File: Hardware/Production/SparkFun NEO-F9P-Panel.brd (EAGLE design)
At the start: 160.8 x 107.4 mm, 768 parts, among them J1 ANTENNA-SMA-GROUNDEDEDGE_SMA, J11 ANTENNA-SMA-GROUNDEDEDGE_SMA, J15 Qwiic Right Angle, J16 Qwiic Right Angle, J18 ANTENNA-SMA-GROUNDEDEDGE_SMA, J2 Qwiic Right Angle, J22 Qwiic Right Angle, J23 Qwiic Right Angle, J25 ANTENNA-SMA-GROUNDEDEDGE_SMA, J29 Qwiic Right Angle, J30 Qwiic Right Angle, J32 ANTENNA-SMA-GROUNDEDEDGE_SMA, J36 Qwiic Right Angle, J37 Qwiic Right Angle, J39 ANTENNA-SMA-GROUNDEDEDGE_SMA, J4 Qwiic Right Angle, J6 Qwiic Right Angle, J9 Qwiic Right Angle, U1 U-BLOX_NEO-F9P-15B, U10 U-BLOX_NEO-F9P-15B, U11 3.3V, U12 U-BLOX_NEO-F9P-15B, U2 3.3V, U3 3.3V, U4 U-BLOX_NEO-F9P-15B, U5 3.3V, U6 U-BLOX_NEO-F9P-15B, U7 3.3V, U8 U-BLOX_NEO-F9P-15B, U9 3.3V

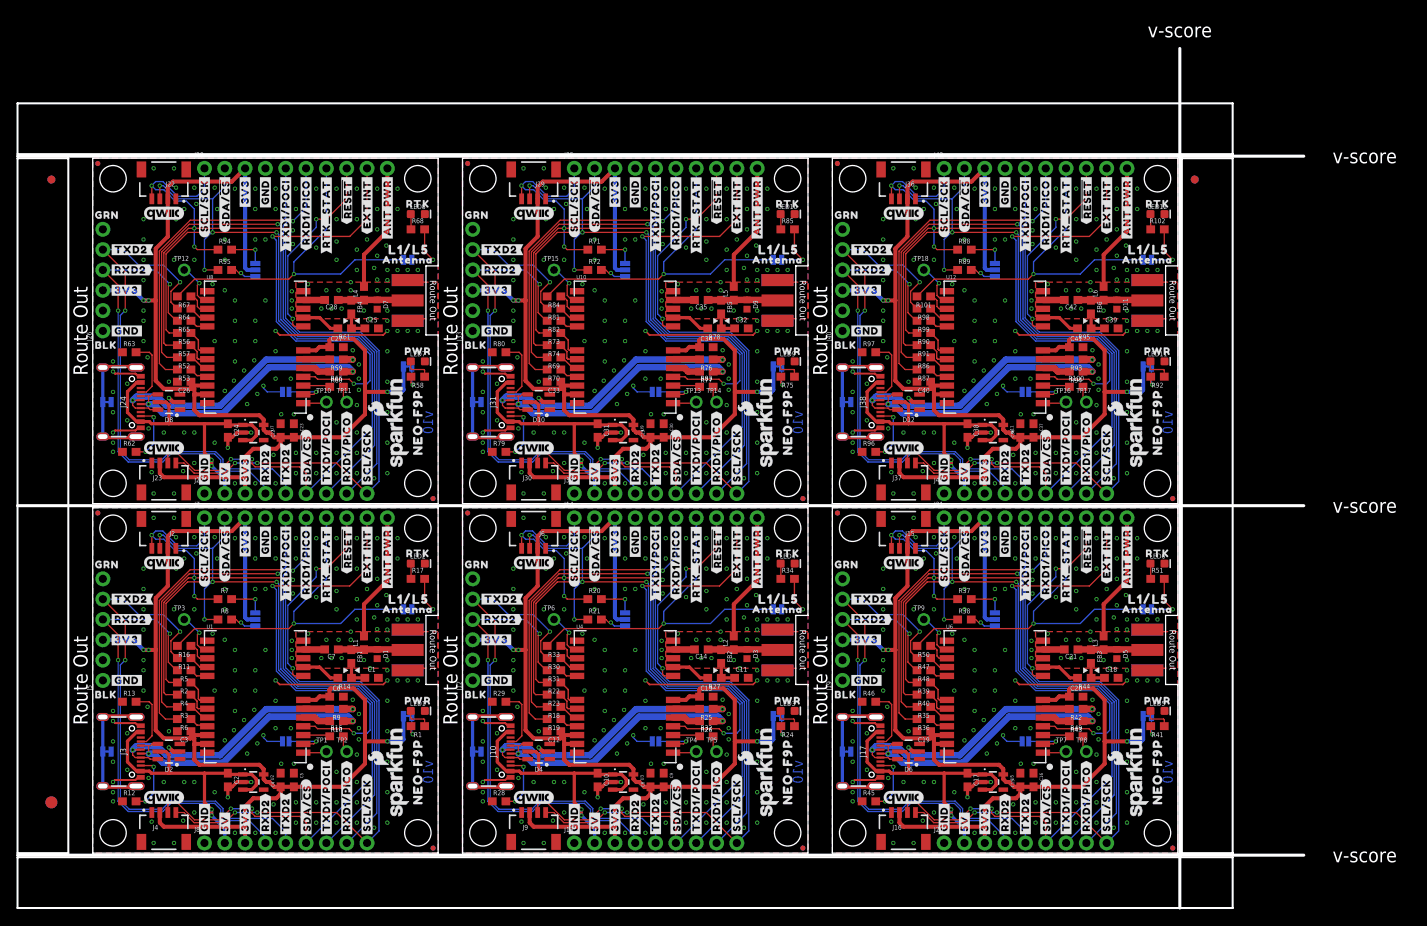
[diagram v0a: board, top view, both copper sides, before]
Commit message: Add backup batt. Add PPS LED and PTH. Change silk. Fix RTK LED.
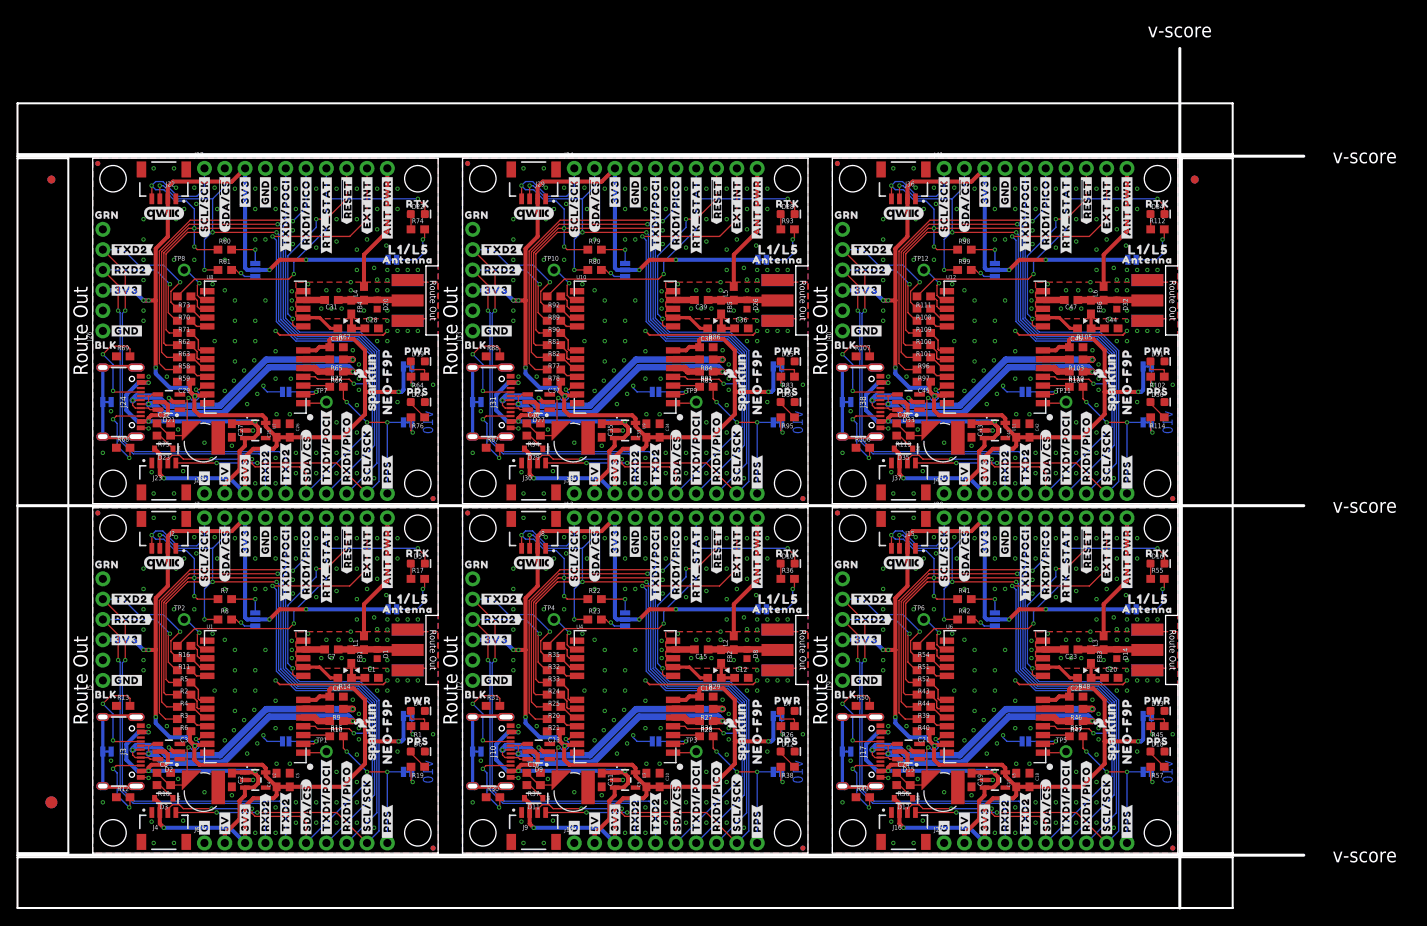
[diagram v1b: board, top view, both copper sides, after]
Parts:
- removed LED1, LED2, LED3, LED4: RED, SparkFun-LED:LED-0603
- removed LOGO25, LOGO29, LOGO30: QWIIC_LOGO_5MM, SparkFun-Aesthetics:QWIIC_5MM
- removed LOGO26, LOGO27: SFE_LOGO_NAME_FLAME.1_INCH, SparkFun-Aesthetics:SFE_LOGO_NAME_FLAME_.1
- removed LOGO28: OSHW-LOGOS, SparkFun-Aesthetics:OSHW-LOGO-S
- removed PWR\10, PWR\11, PWR\6, PWR\7, PWR\8, PWR\9: JUMPER-SMT_2_NC_TRACE_SILK, SparkFun-Jumpers:SMT-JUMPER_2_NC_TRACE_SILK
- removed TP13, TP14, TP15, TP16, TP17, TP18: TEST-POINTPOGO_PTH, SparkFun-Connectors:1X01_NO_SILK
- added B1, B2, B3, B4, B5, B6: 6.8MM_COIN_CELL, SparkFun-Batteries:ML414H_IV01E
- added C43, C45, C46, C48: 1.0uF, SparkFun-Capacitors:0603
- added C44, C47: 47pF, SparkFun-Capacitors:0603@1
- added D14, D20, D26, D32: PESD0402-0402, SparkFun-DiscreteSemi:0402
- added D15, D21, D27, D33: ESD Diode, SparkFun-DiscreteSemi:SOT-23-6
- added D17, D23, D29, D35: 0.5A/40V/420mV, SparkFun-DiscreteSemi:SOD-323
- added D18, D24, D30, D36: Yellow, SparkFun-LED:LED-0603
- added PULSE, PULSE1, PULSE2, PULSE3, PULSE4, PULSE5, RTK, RTK1, RTK2, RTK3, RTK4, RTK5: JUMPER-SMT_2_NC_TRACE_SILK, SparkFun-Jumpers:SMT-JUMPER_2_NC_TRACE_SILK
- added R103, R104: 27, SparkFun-Resistors:0603@1
- added R105: 10, SparkFun-Resistors:0603@1
- added R106, R107: 5.1k, SparkFun-Resistors:0603@1
- added R108, R109, R110, R111: 33, SparkFun-Resistors:0603@1
- added R112, R114: 2.2k, SparkFun-Resistors:0603@1
- added R113: 1k, SparkFun-Resistors:0603
- added U$397, U$398: (no value), output:#RXD1#PICO#2
- added U$399, U$400: (no value), output:#3V3#0
- added U$401: (no value), output:#ANT_PWR#0
- added U$402: (no value), output:#ANT_PWR#1
- added U$403, U$404: (no value), output:NEO#F9P0
- added U$405: (no value), output:#RTK_STAT#0
- added U$406: (no value), output:#_RTK_STAT#0
- added U$407: (no value), output:RTK0
- added U$408: (no value), output:#RTK#0
- added U$409, U$411: (no value), output:L1#L50
- added U$410: (no value), output:ANTENNA0
- added U$412: (no value), output:GNSS_RTK0
- added U$413: (no value), output:RECEIVER0
- added U$414: (no value), output:#LNA_EN#0
- added U$415: (no value), output:PPS0
- added U$416: (no value), output:#PPS#0
- added U$417: (no value), output:#_PPS#0
- added U$418: (no value), output:#PPS_#0
- added U$419: (no value), output:##SAFE##0
- added U$420: (no value), output:#G#0
- C1, C28, C39, C5, C7: device SparkFun-Capacitors:0603 -> SparkFun-Capacitors:0603@1
- C10, C26, C34: value 1.0uF -> 0.1uF; device SparkFun-Capacitors:0603 -> SparkFun-Capacitors:0603@1
- C11, C14, C21, C25, C32, C35: value 47pF -> 1.0uF
- C12, C15, C20, C31, C36: value 1.0uF -> 47pF; device SparkFun-Capacitors:0603 -> SparkFun-Capacitors:0603@1
- C16, C30, C37, C9: value 0.1uF -> 1.0uF
- C18, C42: value 47pF -> 0.1uF; device SparkFun-Capacitors:0603 -> SparkFun-Capacitors:0603@1
- C23: value 0.1uF -> 47pF; device SparkFun-Capacitors:0603 -> SparkFun-Capacitors:0603@1
- D10: value ESD Diode -> Blue; device SparkFun-DiscreteSemi:SOT-23-6 -> SparkFun-LED:LED-0603
- D11, D3: value PESD0402-0402 -> 0.5A/40V/420mV; device SparkFun-DiscreteSemi:0402 -> SparkFun-DiscreteSemi:SOD-323
- D12, D6: value ESD Diode -> Yellow; device SparkFun-DiscreteSemi:SOT-23-6 -> SparkFun-LED:LED-0603
- D13, D19, D25, D31: value RED -> Red
- D16, D22, D28, D34: value RED -> Blue
- D4: value ESD Diode -> Red; device SparkFun-DiscreteSemi:SOT-23-6 -> SparkFun-LED:LED-0603
- D5: value PESD0402-0402 -> Blue; device SparkFun-DiscreteSemi:0402 -> SparkFun-LED:LED-0603
- D7: value PESD0402-0402 -> Red; device SparkFun-DiscreteSemi:0402 -> SparkFun-LED:LED-0603
- D8: value ESD Diode -> PESD0402-0402; device SparkFun-DiscreteSemi:SOT-23-6 -> SparkFun-DiscreteSemi:0402
- D9: value PESD0402-0402 -> ESD Diode; device SparkFun-DiscreteSemi:0402 -> SparkFun-DiscreteSemi:SOT-23-6
- J13, J20, J27, J34, J41: device SparkFun-Connectors:1X09_NO_SILK -> SparkFun-Connectors:1X10_NO_SILK
- J6: value Qwiic Right Angle -> (none); device SparkFun-Connectors:JST04_1MM_RA -> SparkFun-Connectors:1X10_NO_SILK
- J8: value (none) -> Qwiic Right Angle; device SparkFun-Connectors:1X09_NO_SILK -> SparkFun-Connectors:JST04_1MM_RA
- LOGO1, LOGO17, LOGO21, LOGO3: value SFE_LOGO_NAME_FLAME.1_INCH -> SFE_LOGO_NAME_FLAME7_MM; device SparkFun-Aesthetics:SFE_LOGO_NAME_FLAME_.1 -> SparkFun-Aesthetics:SFE_LOGO_NAME_FLAME_7MM
- LOGO10, LOGO14, LOGO6: value QWIIC_LOGO_5MM -> SFE_LOGO_NAME_FLAME.1_INCH; device SparkFun-Aesthetics:QWIIC_5MM -> SparkFun-Aesthetics:SFE_LOGO_NAME_FLAME_.1
- LOGO11, LOGO7: value SFE_LOGO_NAME_FLAME.1_INCH -> OSHW-LOGOS; device SparkFun-Aesthetics:SFE_LOGO_NAME_FLAME_.1 -> SparkFun-Aesthetics:OSHW-LOGO-S
- LOGO12, LOGO16: value SFE_LOGO_NAME_FLAME.1_INCH -> QWIIC_LOGO_5MM; device SparkFun-Aesthetics:SFE_LOGO_NAME_FLAME_.1 -> SparkFun-Aesthetics:QWIIC_5MM
- LOGO13: value OSHW-LOGOS -> SFE_LOGO_NAME_FLAME7_MM; device SparkFun-Aesthetics:OSHW-LOGO-S -> SparkFun-Aesthetics:SFE_LOGO_NAME_FLAME_7MM
- LOGO15, LOGO19: value QWIIC_LOGO_5MM -> OSHW-LOGOS; device SparkFun-Aesthetics:QWIIC_5MM -> SparkFun-Aesthetics:OSHW-LOGO-S
- LOGO18: value OSHW-LOGOS -> SFE_LOGO_NAME_FLAME.1_INCH; device SparkFun-Aesthetics:OSHW-LOGO-S -> SparkFun-Aesthetics:SFE_LOGO_NAME_FLAME_.1
- LOGO8: value OSHW-LOGOS -> QWIIC_LOGO_5MM; device SparkFun-Aesthetics:OSHW-LOGO-S -> SparkFun-Aesthetics:QWIIC_5MM
- LOGO9: value QWIIC_LOGO_5MM -> SFE_LOGO_NAME_FLAME7_MM; device SparkFun-Aesthetics:QWIIC_5MM -> SparkFun-Aesthetics:SFE_LOGO_NAME_FLAME_7MM
- R10, R100, R101, R11, R12, R13, R14, R15, R16, R2, R3, R32, R33, R35, R38, R39, R4, R40, R5, R52, R53, R55, R6, R7, R70, R73, R8, R81, R82, R9, R90, R91: device SparkFun-Resistors:0603 -> SparkFun-Resistors:0603@1
- R17, R41: value 1k -> 2.2k; device SparkFun-Resistors:0603 -> SparkFun-Resistors:0603@1
- R18, R56, R64, R83: value 33 -> 1k
- R19, R22, R23, R36, R57, R74, R98, R99: value 33 -> 2.2k; device SparkFun-Resistors:0603 -> SparkFun-Resistors:0603@1
- R20, R21, R54, R71, R72, R89: value 2.2k -> 33; device SparkFun-Resistors:0603 -> SparkFun-Resistors:0603@1
- R24, R34, R51, R58, R92: value 1k -> 33; device SparkFun-Resistors:0603 -> SparkFun-Resistors:0603@1
- R25, R43, R59, R77: value 27 -> 33; device SparkFun-Resistors:0603 -> SparkFun-Resistors:0603@1
- R26, R94: value 27 -> 1k
- R27: value 10 -> 27; device SparkFun-Resistors:0603 -> SparkFun-Resistors:0603@1
- R28, R46: value 5.1k -> 27; device SparkFun-Resistors:0603 -> SparkFun-Resistors:0603@1
- R29: value 5.1k -> 10; device SparkFun-Resistors:0603 -> SparkFun-Resistors:0603@1
- R30, R31, R49, R50, R69, R87: value 33 -> 5.1k; device SparkFun-Resistors:0603 -> SparkFun-Resistors:0603@1
- R37: value 2.2k -> 1k
- R42, R60, R76, R93: value 27 -> 2.2k; device SparkFun-Resistors:0603 -> SparkFun-Resistors:0603@1
- R44, R78: value 10 -> 33; device SparkFun-Resistors:0603 -> SparkFun-Resistors:0603@1
- R45: value 5.1k -> 1k
- R47, R65, R66, R84: value 33 -> 27; device SparkFun-Resistors:0603 -> SparkFun-Resistors:0603@1
- R48, R67, R86: value 33 -> 10; device SparkFun-Resistors:0603 -> SparkFun-Resistors:0603@1
- R61, R95: value 10 -> 2.2k; device SparkFun-Resistors:0603 -> SparkFun-Resistors:0603@1
- R62, R63, R96, R97: value 5.1k -> 33; device SparkFun-Resistors:0603 -> SparkFun-Resistors:0603@1
- R68: value 1k -> 5.1k; device SparkFun-Resistors:0603 -> SparkFun-Resistors:0603@1
- R79, R80: value 5.1k -> 2.2k; device SparkFun-Resistors:0603 -> SparkFun-Resistors:0603@1
- R85: value 1k -> 27; device SparkFun-Resistors:0603 -> SparkFun-Resistors:0603@1
- R88: value 2.2k -> 5.1k; device SparkFun-Resistors:0603 -> SparkFun-Resistors:0603@1
- U$100: device output:##RESET##1 -> output:#SCL#SCK#1
- U$101: device output:#EXT_INT#0 -> output:#SCL#SCK#1
- U$102: device output:#EXT_INT#1 -> output:##RESET##0
- U$103: device output:PWR0 -> output:##RESET##1
- U$104: device output:#PWR#0 -> output:#EXT_INT#0
- U$105: device output:#SPI#0 -> output:#EXT_INT#1
- U$106: device output:#I�C#0 -> output:PWR0
- U$107: device output:#SHLD#0 -> output:#PWR#0
- U$108: device output:#TXD1#POCI#0 -> output:#SPI#0
- U$109: device output:#TXD1#POCI#0 -> output:#I�C#0
- U$110: device output:#TXD1#POCI#2 -> output:#SHLD#0
- U$111: device output:#TXD1#POCI#2 -> output:#TXD1#POCI#0
- U$112: device output:#RXD1#PICO#0 -> output:#TXD1#POCI#0
- U$113: device output:#RXD1#PICO#0 -> output:#TXD1#POCI#2
- U$114: device output:#RXD1#PICO#2 -> output:#TXD1#POCI#2
- U$115: device output:#RXD1#PICO#2 -> output:#RXD1#PICO#0
- U$116: device output:#3V3#0 -> output:#RXD1#PICO#0
- U$117: device output:#3V3#0 -> output:#RXD1#PICO#2
- U$118: device output:#ANT_PWR#0 -> output:#RXD1#PICO#2
- U$119: device output:#ANT_PWR#1 -> output:#3V3#0
- U$120: device output:NEO#F9P0 -> output:#3V3#0
- U$121: device output:NEO#F9P0 -> output:#ANT_PWR#0
- U$122: device output:#RTK_STAT#0 -> output:#ANT_PWR#1
- U$123: device output:#_RTK_STAT#0 -> output:NEO#F9P0
- U$124: device output:RTK0 -> output:NEO#F9P0
- U$125: device output:##SB##0 -> output:#RTK_STAT#0
- U$126: device output:#PULSE#0 -> output:#_RTK_STAT#0
- U$127: device output:#RTK#0 -> output:RTK0
- U$128: device output:L1#L50 -> output:#RTK#0
- U$129: device output:ANTENNA0 -> output:L1#L50
- U$130: device output:L1#L50 -> output:ANTENNA0
- U$131: device output:GNSS_RTK0 -> output:L1#L50
- U$132: device output:RECEIVER0 -> output:GNSS_RTK0
- U$133: device output:#GND#0 -> output:RECEIVER0
- U$134, U$67: device output:#GND#0 -> output:#LNA_EN#0
- U$135, U$68: device output:#GND#0 -> output:PPS0
- U$136: device output:#GND#1 -> output:#PPS#0
- U$137, U$70: device output:#GND#1 -> output:#_PPS#0
- U$138, U$71: device output:#GND#1 -> output:#PPS_#0
- U$139: device output:#TXD2#0 -> output:##SAFE##0
- U$140: device output:#TXD2#0 -> output:#G#0
- U$141, U$142: device output:#TXD2#3 -> output:#GND#0
- U$143, U$144: device output:#RXD2#0 -> output:#GND#1
- U$145: device output:#RXD2#3 -> output:#GND#1
- U$146: device output:#RXD2#3 -> output:#TXD2#0
- U$147: device output:BLK0 -> output:#TXD2#0
- U$148: device output:BLK0 -> output:#TXD2#3
- U$149: device output:GRN0 -> output:#TXD2#3
- U$150: device output:GRN0 -> output:#RXD2#0
- U$151: device output:#5V#0 -> output:#RXD2#0
- U$152: device output:#5V#6 -> output:#RXD2#3
- U$153: device output:#3V3#0 -> output:#RXD2#3
- U$154: device output:#3V3#0 -> output:BLK0
- U$155: device output:#3V3#4 -> output:BLK0
- U$156: device output:#3V3#4 -> output:GRN0
- U$157: device output:#SDA##CS##0 -> output:GRN0
- U$158: device output:#SDA##CS##0 -> output:#5V#0
- U$159: device output:#SDA##CS##1 -> output:#5V#6
- U$160: device output:#SDA##CS##1 -> output:#3V3#0
- U$161: device output:#SCL#SCK#0 -> output:#3V3#0
- U$162: device output:#SCL#SCK#0 -> output:#3V3#4
- U$163: device output:#SCL#SCK#1 -> output:#3V3#4
- U$164: device output:#SCL#SCK#1 -> output:#SDA##CS##0
- U$165: device output:##RESET##0 -> output:#SDA##CS##0
- U$166: device output:##RESET##1 -> output:#SDA##CS##1
- U$167: device output:#EXT_INT#0 -> output:#SDA##CS##1
- U$168: device output:#EXT_INT#1 -> output:#SCL#SCK#0
- U$169: device output:PWR0 -> output:#SCL#SCK#0
- U$170: device output:#PWR#0 -> output:#SCL#SCK#1
- U$171: device output:#SPI#0 -> output:#SCL#SCK#1
- U$172: device output:#I�C#0 -> output:##RESET##0
- U$173: device output:#SHLD#0 -> output:##RESET##1
- U$174: device output:#TXD1#POCI#0 -> output:#EXT_INT#0
- U$175: device output:#TXD1#POCI#0 -> output:#EXT_INT#1
- U$176: device output:#TXD1#POCI#2 -> output:PWR0
- U$177: device output:#TXD1#POCI#2 -> output:#PWR#0
- U$178: device output:#RXD1#PICO#0 -> output:#SPI#0
- U$179: device output:#RXD1#PICO#0 -> output:#I�C#0
- U$180: device output:#RXD1#PICO#2 -> output:#SHLD#0
- U$181: device output:#RXD1#PICO#2 -> output:#TXD1#POCI#0
- U$182: device output:#3V3#0 -> output:#TXD1#POCI#0
- U$183: device output:#3V3#0 -> output:#TXD1#POCI#2
- U$184: device output:#ANT_PWR#0 -> output:#TXD1#POCI#2
- U$185: device output:#ANT_PWR#1 -> output:#RXD1#PICO#0
- U$186: device output:NEO#F9P0 -> output:#RXD1#PICO#0
- U$187: device output:NEO#F9P0 -> output:#RXD1#PICO#2
- U$188: device output:#RTK_STAT#0 -> output:#RXD1#PICO#2
- U$189: device output:#_RTK_STAT#0 -> output:#3V3#0
- U$190: device output:RTK0 -> output:#3V3#0
- U$191: device output:##SB##0 -> output:#ANT_PWR#0
- U$192: device output:#PULSE#0 -> output:#ANT_PWR#1
- U$193: device output:#RTK#0 -> output:NEO#F9P0
- U$194: device output:L1#L50 -> output:NEO#F9P0
- U$195: device output:ANTENNA0 -> output:#RTK_STAT#0
- U$196: device output:L1#L50 -> output:#_RTK_STAT#0
- U$197: device output:GNSS_RTK0 -> output:RTK0
- U$198: device output:RECEIVER0 -> output:#RTK#0
- U$199, U$201: device output:#GND#0 -> output:L1#L50
- U$200: device output:#GND#0 -> output:ANTENNA0
- U$202: device output:#GND#1 -> output:GNSS_RTK0
- U$203: device output:#GND#1 -> output:RECEIVER0
- U$204: device output:#GND#1 -> output:#LNA_EN#0
- U$205: device output:#TXD2#0 -> output:PPS0
- U$206: device output:#TXD2#0 -> output:#PPS#0
- U$207: device output:#TXD2#3 -> output:#_PPS#0
- U$208: device output:#TXD2#3 -> output:#PPS_#0
- U$209: device output:#RXD2#0 -> output:##SAFE##0
- U$210: device output:#RXD2#0 -> output:#G#0
- U$211, U$212: device output:#RXD2#3 -> output:#GND#0
- U$213, U$214: device output:BLK0 -> output:#GND#1
- U$215: device output:GRN0 -> output:#GND#1
- U$216: device output:GRN0 -> output:#TXD2#0
- U$217: device output:#5V#0 -> output:#TXD2#0
- U$218: device output:#5V#6 -> output:#TXD2#3
- U$219: device output:#3V3#0 -> output:#TXD2#3
- U$220: device output:#3V3#0 -> output:#RXD2#0
- U$221: device output:#3V3#4 -> output:#RXD2#0
- U$222: device output:#3V3#4 -> output:#RXD2#3
- U$223: device output:#SDA##CS##0 -> output:#RXD2#3
- U$224: device output:#SDA##CS##0 -> output:BLK0
- U$225: device output:#SDA##CS##1 -> output:BLK0
- U$226: device output:#SDA##CS##1 -> output:GRN0
- U$227: device output:#SCL#SCK#0 -> output:GRN0
- U$228: device output:#SCL#SCK#0 -> output:#5V#0
- U$229: device output:#SCL#SCK#1 -> output:#5V#6
- U$230: device output:#SCL#SCK#1 -> output:#3V3#0
- U$231: device output:##RESET##0 -> output:#3V3#0
- U$232: device output:##RESET##1 -> output:#3V3#4
- U$233: device output:#EXT_INT#0 -> output:#3V3#4
- U$234: device output:#EXT_INT#1 -> output:#SDA##CS##0
- U$235: device output:PWR0 -> output:#SDA##CS##0
- U$236: device output:#PWR#0 -> output:#SDA##CS##1
- U$237: device output:#SPI#0 -> output:#SDA##CS##1
- U$238: device output:#I�C#0 -> output:#SCL#SCK#0
- U$239: device output:#SHLD#0 -> output:#SCL#SCK#0
- U$240, U$241: device output:#TXD1#POCI#0 -> output:#SCL#SCK#1
- U$242: device output:#TXD1#POCI#2 -> output:##RESET##0
- U$243: device output:#TXD1#POCI#2 -> output:##RESET##1
- U$244: device output:#RXD1#PICO#0 -> output:#EXT_INT#0
- U$245: device output:#RXD1#PICO#0 -> output:#EXT_INT#1
- U$246: device output:#RXD1#PICO#2 -> output:PWR0
- U$247: device output:#RXD1#PICO#2 -> output:#PWR#0
- U$248: device output:#3V3#0 -> output:#SPI#0
- U$249: device output:#3V3#0 -> output:#I�C#0
- U$250: device output:#ANT_PWR#0 -> output:#SHLD#0
- U$251: device output:#ANT_PWR#1 -> output:#TXD1#POCI#0
- U$252: device output:NEO#F9P0 -> output:#TXD1#POCI#0
- U$253: device output:NEO#F9P0 -> output:#TXD1#POCI#2
- U$254: device output:#RTK_STAT#0 -> output:#TXD1#POCI#2
- U$255: device output:#_RTK_STAT#0 -> output:#RXD1#PICO#0
- U$256: device output:RTK0 -> output:#RXD1#PICO#0
- U$257: device output:##SB##0 -> output:#RXD1#PICO#2
- U$258: device output:#PULSE#0 -> output:#RXD1#PICO#2
- U$259: device output:#RTK#0 -> output:#3V3#0
- U$260: device output:L1#L50 -> output:#3V3#0
- U$261: device output:ANTENNA0 -> output:#ANT_PWR#0
- U$262: device output:L1#L50 -> output:#ANT_PWR#1
- U$263: device output:GNSS_RTK0 -> output:NEO#F9P0
- U$264: device output:RECEIVER0 -> output:NEO#F9P0
- U$265: device output:#GND#0 -> output:#RTK_STAT#0
- U$266: device output:#GND#0 -> output:#_RTK_STAT#0
- U$267: device output:#GND#0 -> output:RTK0
- U$268: device output:#GND#1 -> output:#RTK#0
- U$269: device output:#GND#1 -> output:L1#L50
- U$270: device output:#GND#1 -> output:ANTENNA0
- U$271: device output:#TXD2#0 -> output:L1#L50
- U$272: device output:#TXD2#0 -> output:GNSS_RTK0
- U$273: device output:#TXD2#3 -> output:RECEIVER0
- U$274: device output:#TXD2#3 -> output:#LNA_EN#0
- U$275: device output:#RXD2#0 -> output:PPS0
- U$276: device output:#RXD2#0 -> output:#PPS#0
- U$277: device output:#RXD2#3 -> output:#_PPS#0
- U$278: device output:#RXD2#3 -> output:#PPS_#0
- U$279: device output:BLK0 -> output:##SAFE##0
- U$280: device output:BLK0 -> output:#G#0
- U$281, U$282: device output:GRN0 -> output:#GND#0
- U$283: device output:#5V#0 -> output:#GND#1
- U$284: device output:#5V#6 -> output:#GND#1
- U$285: device output:#3V3#0 -> output:#GND#1
- U$286: device output:#3V3#0 -> output:#TXD2#0
- U$287: device output:#3V3#4 -> output:#TXD2#0
- U$288: device output:#3V3#4 -> output:#TXD2#3
- U$289: device output:#SDA##CS##0 -> output:#TXD2#3
- U$290: device output:#SDA##CS##0 -> output:#RXD2#0
- U$291: device output:#SDA##CS##1 -> output:#RXD2#0
- U$292: device output:#SDA##CS##1 -> output:#RXD2#3
- U$293: device output:#SCL#SCK#0 -> output:#RXD2#3
- U$294: device output:#SCL#SCK#0 -> output:BLK0
- U$295: device output:#SCL#SCK#1 -> output:BLK0
- U$296: device output:#SCL#SCK#1 -> output:GRN0
- U$297: device output:##RESET##0 -> output:GRN0
- U$298: device output:##RESET##1 -> output:#5V#0
- U$299: device output:#EXT_INT#0 -> output:#5V#6
- U$300: device output:#EXT_INT#1 -> output:#3V3#0
- U$301: device output:PWR0 -> output:#3V3#0
- U$302: device output:#PWR#0 -> output:#3V3#4
- U$303: device output:#SPI#0 -> output:#3V3#4
- U$304: device output:#I�C#0 -> output:#SDA##CS##0
- U$305: device output:#SHLD#0 -> output:#SDA##CS##0
- U$306, U$307: device output:#TXD1#POCI#0 -> output:#SDA##CS##1
- U$308, U$309: device output:#TXD1#POCI#2 -> output:#SCL#SCK#0
- U$310, U$311: device output:#RXD1#PICO#0 -> output:#SCL#SCK#1
- U$312: device output:#RXD1#PICO#2 -> output:##RESET##0
- U$313: device output:#RXD1#PICO#2 -> output:##RESET##1
- U$314: device output:#3V3#0 -> output:#EXT_INT#0
- U$315: device output:#3V3#0 -> output:#EXT_INT#1
- U$316: device output:#ANT_PWR#0 -> output:PWR0
- U$317: device output:#ANT_PWR#1 -> output:#PWR#0
- U$318: device output:NEO#F9P0 -> output:#SPI#0
- U$319: device output:NEO#F9P0 -> output:#I�C#0
- U$320: device output:#RTK_STAT#0 -> output:#SHLD#0
- U$321: device output:#_RTK_STAT#0 -> output:#TXD1#POCI#0
- U$322: device output:RTK0 -> output:#TXD1#POCI#0
- U$323: device output:##SB##0 -> output:#TXD1#POCI#2
- U$324: device output:#PULSE#0 -> output:#TXD1#POCI#2
- U$325: device output:#RTK#0 -> output:#RXD1#PICO#0
- U$326: device output:L1#L50 -> output:#RXD1#PICO#0
- U$327: device output:ANTENNA0 -> output:#RXD1#PICO#2
- U$328: device output:L1#L50 -> output:#RXD1#PICO#2
- U$329: device output:GNSS_RTK0 -> output:#3V3#0
- U$330: device output:RECEIVER0 -> output:#3V3#0
- U$331: device output:#GND#0 -> output:#ANT_PWR#0
- U$332: device output:#GND#0 -> output:#ANT_PWR#1
- U$333: device output:#GND#0 -> output:NEO#F9P0
- U$334: device output:#GND#1 -> output:NEO#F9P0
- U$335: device output:#GND#1 -> output:#RTK_STAT#0
- U$336: device output:#GND#1 -> output:#_RTK_STAT#0
- U$337: device output:#TXD2#0 -> output:RTK0
- U$338: device output:#TXD2#0 -> output:#RTK#0
- U$339: device output:#TXD2#3 -> output:L1#L50
- U$340: device output:#TXD2#3 -> output:ANTENNA0
- U$341: device output:#RXD2#0 -> output:L1#L50
- U$342: device output:#RXD2#0 -> output:GNSS_RTK0
- U$343: device output:#RXD2#3 -> output:RECEIVER0
- U$344: device output:#RXD2#3 -> output:#LNA_EN#0
- U$345: device output:BLK0 -> output:PPS0
- U$346: device output:BLK0 -> output:#PPS#0
- U$347: device output:GRN0 -> output:#_PPS#0
- U$348: device output:GRN0 -> output:#PPS_#0
- U$349: device output:#5V#0 -> output:##SAFE##0
- U$350: device output:#5V#6 -> output:#G#0
- U$351, U$352: device output:#3V3#0 -> output:#GND#0
- U$353, U$354: device output:#3V3#4 -> output:#GND#1
- U$355: device output:#SDA##CS##0 -> output:#GND#1
- U$356: device output:#SDA##CS##0 -> output:#TXD2#0
- U$357: device output:#SDA##CS##1 -> output:#TXD2#0
- U$358: device output:#SDA##CS##1 -> output:#TXD2#3
- U$359: device output:#SCL#SCK#0 -> output:#TXD2#3
- U$360: device output:#SCL#SCK#0 -> output:#RXD2#0
- U$361: device output:#SCL#SCK#1 -> output:#RXD2#0
- U$362: device output:#SCL#SCK#1 -> output:#RXD2#3
- U$363: device output:##RESET##0 -> output:#RXD2#3
- U$364: device output:##RESET##1 -> output:BLK0
- U$365: device output:#EXT_INT#0 -> output:BLK0
- U$366: device output:#EXT_INT#1 -> output:GRN0
- U$367: device output:PWR0 -> output:GRN0
- U$368: device output:#PWR#0 -> output:#5V#0
- U$369: device output:#SPI#0 -> output:#5V#6
- U$370: device output:#I�C#0 -> output:#3V3#0
- U$371: device output:#SHLD#0 -> output:#3V3#0
- U$372, U$373: device output:#TXD1#POCI#0 -> output:#3V3#4
- U$374, U$375: device output:#TXD1#POCI#2 -> output:#SDA##CS##0
- U$376, U$377: device output:#RXD1#PICO#0 -> output:#SDA##CS##1
- U$378, U$379: device output:#RXD1#PICO#2 -> output:#SCL#SCK#0
- U$380, U$381: device output:#3V3#0 -> output:#SCL#SCK#1
- U$382: device output:#ANT_PWR#0 -> output:##RESET##0
- U$383: device output:#ANT_PWR#1 -> output:##RESET##1
- U$384: device output:NEO#F9P0 -> output:#EXT_INT#0
- U$385: device output:NEO#F9P0 -> output:#EXT_INT#1
- U$386: device output:#RTK_STAT#0 -> output:PWR0
- U$387: device output:#_RTK_STAT#0 -> output:#PWR#0
- U$388: device output:RTK0 -> output:#SPI#0
- U$389: device output:##SB##0 -> output:#I�C#0
- U$390: device output:#PULSE#0 -> output:#SHLD#0
- U$391: device output:#RTK#0 -> output:#TXD1#POCI#0
- U$392: device output:L1#L50 -> output:#TXD1#POCI#0
- U$393: device output:ANTENNA0 -> output:#TXD1#POCI#2
- U$394: device output:L1#L50 -> output:#TXD1#POCI#2
- U$395: device output:GNSS_RTK0 -> output:#RXD1#PICO#0
- U$396: device output:RECEIVER0 -> output:#RXD1#PICO#0
- U$55: device output:##SB##0 -> output:#G#0
- U$62: device output:#PULSE#0 -> output:#GND#0
- U$69: device output:#GND#0 -> output:#PPS#0
- U$72: device output:#GND#1 -> output:##SAFE##0
- U$73, U$74: device output:#TXD2#0 -> output:#GND#1
- U$75: device output:#TXD2#3 -> output:#GND#1
- U$76: device output:#TXD2#3 -> output:#TXD2#0
- U$77: device output:#RXD2#0 -> output:#TXD2#0
- U$78: device output:#RXD2#0 -> output:#TXD2#3
- U$79: device output:#RXD2#3 -> output:#TXD2#3
- U$80: device output:#RXD2#3 -> output:#RXD2#0
- U$81: device output:BLK0 -> output:#RXD2#0
- U$82: device output:BLK0 -> output:#RXD2#3
- U$83: device output:GRN0 -> output:#RXD2#3
- U$84: device output:GRN0 -> output:BLK0
- U$85: device output:#5V#0 -> output:BLK0
- U$86: device output:#5V#6 -> output:GRN0
- U$87: device output:#3V3#0 -> output:GRN0
- U$88: device output:#3V3#0 -> output:#5V#0
- U$89: device output:#3V3#4 -> output:#5V#6
- U$90: device output:#3V3#4 -> output:#3V3#0
- U$91: device output:#SDA##CS##0 -> output:#3V3#0
- U$92: device output:#SDA##CS##0 -> output:#3V3#4
- U$93: device output:#SDA##CS##1 -> output:#3V3#4
- U$94: device output:#SDA##CS##1 -> output:#SDA##CS##0
- U$95: device output:#SCL#SCK#0 -> output:#SDA##CS##0
- U$96: device output:#SCL#SCK#0 -> output:#SDA##CS##1
- U$97: device output:#SCL#SCK#1 -> output:#SDA##CS##1
- U$98: device output:#SCL#SCK#1 -> output:#SCL#SCK#0
- U$99: device output:##RESET##0 -> output:#SCL#SCK#0
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- renumbered LED10 to D28, LED11 to D31, LED12 to D34, LED5 to D13, LED6 to D16, LED7 to D19, LED8 to D22, LED9 to D25
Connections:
- removed net N$103 (its old number): J38.A5, R97.2
- removed net N$37 (its old number): LED4.A, R34.1
- removed net N$59 (its old number): I2C3.3, R54.2
- removed net N$81 (its old number): R77.2, U10.5
- new net BACKUP: B1.+, C8.1, R18.1, U1.22
- new net BACKUP1: B2.+, C16.1, R37.1, U4.22
- new net BACKUP2: B3.+, C24.1, R56.1, U6.22
- new net BACKUP3: B4.+, C32.1, R75.1, U8.22
- new net BACKUP4: B5.+, C40.1, R94.1, U10.22
- new net BACKUP5: B6.+, C48.1, R113.1, U12.22
- new net N$110: PULSE4.1, R95.2
- new net N$115: R104.2, U12.5
- new net N$116: PWR\5.1, R102.2
- new net N$117: J38.B5, R106.2
- new net N$118: J38.A5, R107.2
- new net N$119: R108.1, U12.16
- new net N$120: R109.1, U12.17
- new net N$121: R96.1, U12.20
- new net N$122: R97.1, U12.21
- new net N$123: R100.1, U12.18
- new net N$124: R101.1, U12.19
- new net N$126: R110.1, U12.3
- new net N$127: R111.1, U12.15
- new net N$128: D34.A, R112.1
- new net N$129: R112.2, RTK5.1
- new net N$130: D35.C, R113.2
- new net N$131: D36.A, R114.1
- new net N$132: PULSE5.1, R114.2
- new net N$34: R21.1, U4.21
- new net N$53: R51.1, U6.16
- new net N$72: PWR\3.1, R64.2
- new net N$91: D25.A, R83.1
- net !RESET!1: now also J13.8; no longer J14.8
- net !RESET!2: now also J20.8; no longer J21.8
- net !RESET!3: now also J27.8; no longer J28.8
- net !RESET!4: now also J34.8; no longer J35.8
- net !RESET!5: now also J41.8; no longer J42.8
- net !SAFEBOOT!1: now also TP3.1; no longer TP4.1
- net !SAFEBOOT!2: now also TP5.1; no longer TP7.1
- net !SAFEBOOT!3: now also TP7.1; no longer TP10.1
- net !SAFEBOOT!4: now also TP9.1; no longer TP13.1
- net !SAFEBOOT!5: now also TP11.1; no longer TP16.1
- net 3.3V: now also D3.A, J6.3, RTK.2; no longer J8.3, U1.22
- net 3.3V1: now also C10.2, C14.1, C9.1, D11.A, J8.2, PWR\1.2, RTK1.2; no longer C12.1, C8.1, C9.2, J6.2, PWR\2.2, U4.22
- net 3.3V2: now also C17.1, C18.2, C21.1, C22.1, D17.A, PWR\2.2, RTK2.2; no longer C15.1, C16.2, C19.1, C20.1, PWR\4.2, U6.22
- net 3.3V3: now also C25.1, C26.2, C29.1, C30.1, D23.A, PWR\3.2, RTK3.2; no longer C22.1, C23.2, C26.1, C27.1, PWR\6.2, U8.22
- net 3.3V4: now also C34.2, C37.1, C38.1, D29.A, PWR\4.2, RTK4.2; no longer C29.1, C30.2, C34.1, PWR\8.2, U10.22
- net 3.3V5: now also C42.2, C45.1, C46.1, D35.A, PWR\5.2, RTK5.2; no longer C36.1, C37.2, C40.1, PWR\10.2, U12.22
- net 5V: now also J6.2; no longer J8.2
- net 5V1: now also C11.1, D9.5, J14.2; no longer C10.1, D4.5, J13.2
- net 5V2: now also C19.1, D15.5, J21.2; no longer C17.1, D6.5, J20.2
- net 5V3: now also C27.1, D21.5, J28.2; no longer C24.1, D8.5, J27.2
- net 5V4: now also C35.1, D27.5, J35.2; no longer C31.1, D10.5, J34.2
- net 5V5: now also C43.1, D33.5, J42.2; no longer C38.1, D12.5, J41.2
- net ANT1: now also C15.2; no longer C14.2
- net ANT2: now also C23.2; no longer C21.2
- net ANT3: now also C31.2; no longer C28.2
- net ANT4: now also C39.2; no longer C35.2
- net ANT5: now also C47.2; no longer C42.2
- net ANT_PWR1: now also J13.10; no longer J14.10
- net ANT_PWR2: now also J20.10; no longer J21.10
- net ANT_PWR3: now also J27.10; no longer J28.10
- net ANT_PWR4: now also J34.10; no longer J35.10
- net ANT_PWR5: now also J41.10; no longer J42.10
- net ANT_VCC1: now also C12.1, R29.1; no longer C11.1, R27.1
- net ANT_VCC2: now also C20.1, R48.1; no longer C18.1, R44.1
- net ANT_VCC3: now also C28.1, R67.1; no longer C25.1, R61.1
- net ANT_VCC4: now also C36.1, R86.1; no longer C32.1, R78.1
- net ANT_VCC5: now also C44.1, R105.1; no longer C39.1, R95.1
- net D+1: now also D9.6, R27.1; no longer D4.6, R25.1
- net D+2: now also D15.6, R46.1; no longer D6.6, R42.1
- net D+3: now also D21.6, R65.1; no longer D8.6, R59.1
- net D+4: now also D27.6, R84.1; no longer D10.6, R76.1
- net D+5: now also D33.6, R103.1; no longer D12.6, R93.1
- net D-1: now also D9.4, R28.1; no longer D4.4, R26.1
- net D-2: now also D15.4, R47.1; no longer D6.4, R43.1
- net D-3: now also D21.4, R66.1; no longer D8.4, R60.1
- net D-4: now also D27.4, R85.1; no longer D10.4, R77.1
- net D-5: now also D33.4, R104.1; no longer D12.4, R94.1
- net EXT_INT1: now also J13.9; no longer J14.9
- net EXT_INT2: now also J20.9; no longer J21.9
- net EXT_INT3: now also J27.9; no longer J28.9
- net EXT_INT4: now also J34.9; no longer J35.9
- net EXT_INT5: now also J41.9; no longer J42.9
- net GND: now also B1.-, C8.2, D4.C, D6.C, J6.1; no longer J8.1, LED1.C, LED2.C
- net GND1: now also B2.-, C10.1, C14.2, C16.2, C9.2, D12.C, D7.C, D8.2, D9.2, J13.4, J14.1, J8.1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; no longer C10.2, C8.2, C9.1, D3.2, D4.2, J13.1, J14.4, J6.1, LED3.C, LED4.C, R28.1, R29.1
- net GND2: now also B3.-, C18.1, C21.2, C22.2, C24.2, D14.2, D15.2, D18.C, J20.4, J21.1, R49.1, R50.1; no longer C15.2, C16.1, C18.2, D16.C, D5.2, D6.2, J20.1, J21.4, R45.1, R46.1
- net GND3: now also B4.-, C26.1, C28.2, C29.2, C30.2, C32.2, D20.2, D21.2, D24.C, J27.4, J28.1, R68.1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; no longer C22.2, C23.1, C24.2, C26.2, D22.C, D7.2, D8.2, J27.1, J28.4, R62.1, R63.1
- net GND4: now also B5.-, C34.1, C35.2, C36.2, C37.2, C38.2, C40.2, D26.2, D27.2, D30.C, J34.4, J35.1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; no longer C29.2, C30.1, C31.2, C32.2, C34.2, D10.2, D28.C, D9.2, J34.1, J35.4, R79.1, R80.1
- net GND5: now also B6.-, C42.1, C43.2, C44.2, C45.2, C46.2, C48.2, D32.2, D33.2, D36.C, J41.4, J42.1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; no longer C36.2, C37.1, C38.2, C39.2, C40.2, D11.2, D12.2, D34.C, J41.1, J42.4, R96.1, R97.1
- net LNA_EN: now also TP2.1; no longer TP3.1
- net LNA_EN1: now also TP4.1; no longer TP6.1
- net LNA_EN2: now also TP6.1; no longer TP9.1
- net LNA_EN3: now also TP8.1; no longer TP12.1
- net LNA_EN4: now also TP10.1; no longer TP15.1
- net LNA_EN5: now also TP12.1; no longer TP18.1
- net N$10: now also D4.A; no longer LED1.A
- net N$100: now also R78.1, U10.21; no longer R94.2, U12.5
- net N$101: now also R81.1, U10.18; no longer PWR\10.1, R92.2
- net N$102: now also R82.1, U10.19; no longer J38.B5, R96.2
- net N$104: now also R91.1, U10.3; no longer R98.1, U12.16
- net N$105: now also R92.1, U10.15; no longer R99.1, U12.17
- net N$106: now also D28.A, R93.1; no longer R86.1, U12.20
- net N$107: now also R93.2, RTK4.1; no longer R87.1, U12.21
- net N$108: now also D29.C, R94.2; no longer R90.1, U12.18
- net N$109: now also D30.A, R95.1; no longer R91.1, U12.19
- net N$111: now also I2C5.1, R99.2; no longer R100.1, U12.3
- net N$112: now also I2C5.3, R98.2; no longer R101.1, U12.15
- net N$113: now also D31.A; no longer D34.A
- net N$114: now also R103.2, U12.6; no longer PWR\11.1, R102.2
- net N$18: now also D5.A; no longer LED2.A
- net N$19: now also RTK.1; no longer PWR\1.1
- net N$20: now also D3.C, R18.2; no longer I2C1.1, R21.2
- net N$21: now also D6.A, R19.1; no longer I2C1.3, R20.2
- net N$22: now also PULSE.1, R19.2; no longer LED3.A, R24.1
- net N$23: now also I2C1.1, R23.2; no longer R25.2, U4.6
- net N$24: now also I2C1.3, R22.2; no longer R26.2, U4.5
- net N$25: now also D7.A, R26.1; no longer PWR\2.1, R24.2
- net N$26: now also R27.2, U4.6; no longer J10.B5, R28.2
- net N$27: now also R28.2, U4.5; no longer J10.A5, R29.2
- net N$28: now also PWR\1.1, R26.2; no longer R30.1, U4.16
- net N$29: now also J10.B5, R30.2; no longer R31.1, U4.17
- net N$30: now also J10.A5, R31.2; no longer R18.1, U4.20
- net N$31: now also R32.1, U4.16; no longer R19.1, U4.21
- net N$32: now also R33.1, U4.17; no longer R22.1, U4.18
- net N$33: now also R20.1, U4.20; no longer R23.1, U4.19
- net N$35: now also R24.1, U4.18; no longer R32.1, U4.3
- net N$36: now also R25.1, U4.19; no longer R33.1, U4.15
- net N$38: now also R34.1, U4.3; no longer PWR\3.1, R34.2
- net N$39: now also R35.1, U4.15; no longer I2C2.1, R38.2
- net N$40: now also D10.A, R36.1; no longer I2C2.3, R37.2
- net N$41: now also R36.2, RTK1.1; no longer D13.A, R41.1
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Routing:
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
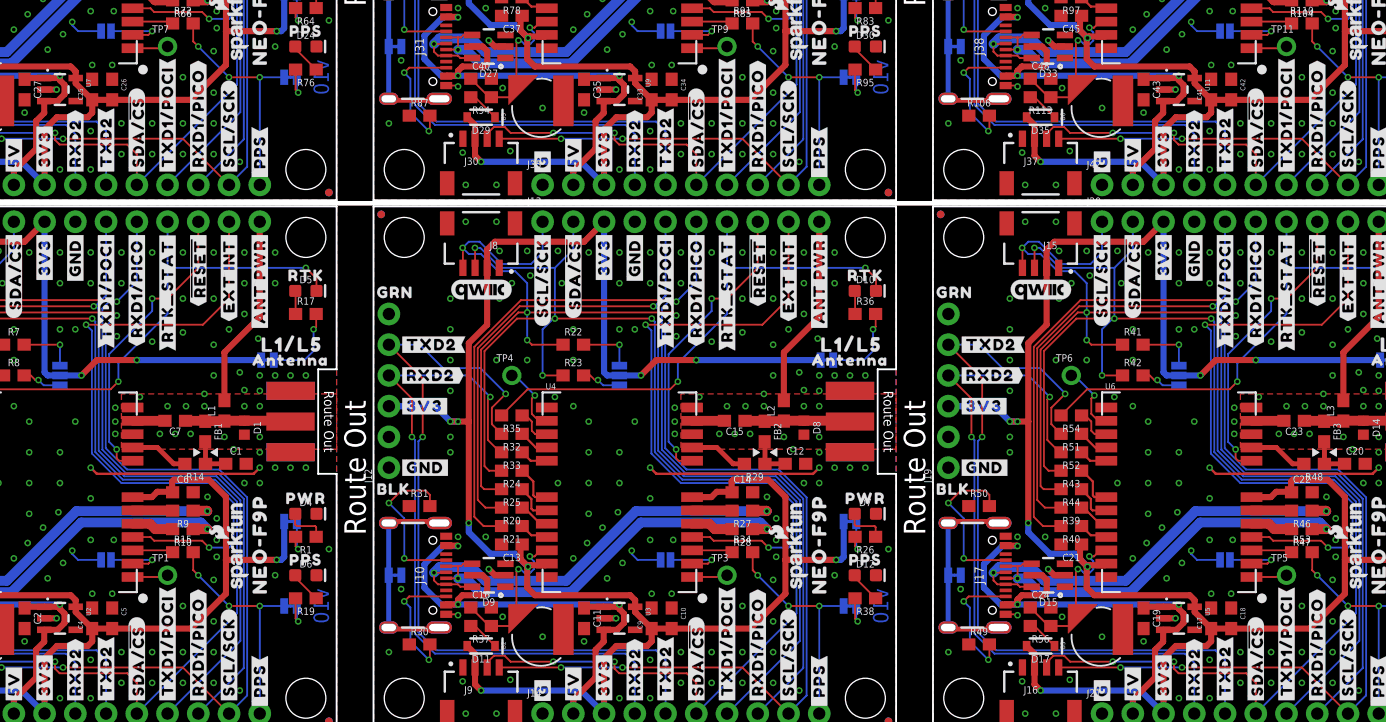
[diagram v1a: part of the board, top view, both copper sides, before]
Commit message: Move R2.
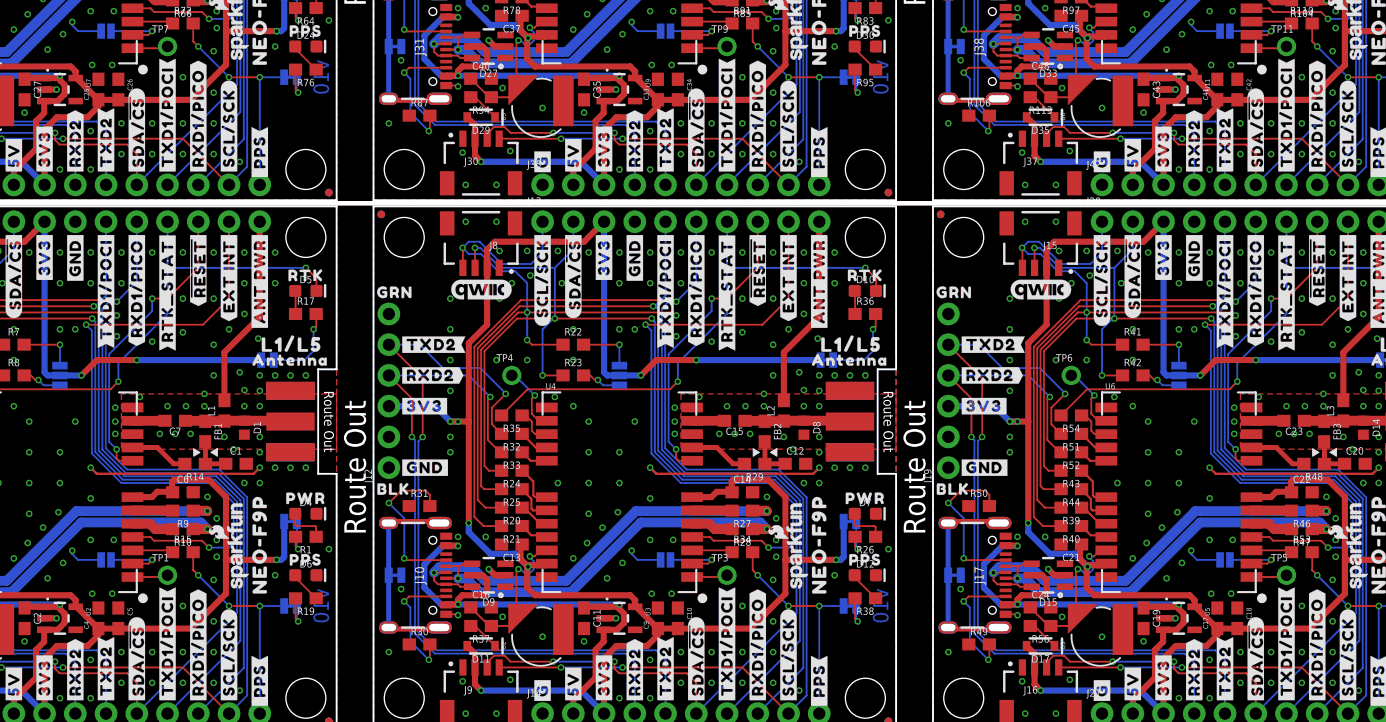
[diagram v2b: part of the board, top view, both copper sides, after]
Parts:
- moved C18 0.51 mm to (117.6, 9.14)
- moved C42 0.51 mm to (117.6, 52.8)
- moved C25 0.51 mm to (23.5, 52.8)
- moved C4 0.51 mm to (23.5, 9.14)
- moved C26 0.51 mm to (25.1, 52.8)
- moved C5 0.51 mm to (25.1, 9.14)
- moved C10 0.51 mm to (71.4, 9.14)
- moved C17 0.51 mm to (116.0, 9.14)
- moved C33 0.51 mm to (69.7, 52.8)
- moved C34 0.51 mm to (71.4, 52.8)
- moved C41 0.51 mm to (116.0, 52.8)
- moved C9 0.51 mm to (69.7, 9.14)
